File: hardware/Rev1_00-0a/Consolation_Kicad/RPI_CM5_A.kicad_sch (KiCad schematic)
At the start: 56 parts, among them J19 RPI_CMx_A, J7 2998TR, Q12 2N7002, Q13 2N7002, Q15 2N7002, Q16 2N7002, U19 SN74LVC1G125DBVR, U21 MCP7940NT-I/MS, Y2 32.768kHz

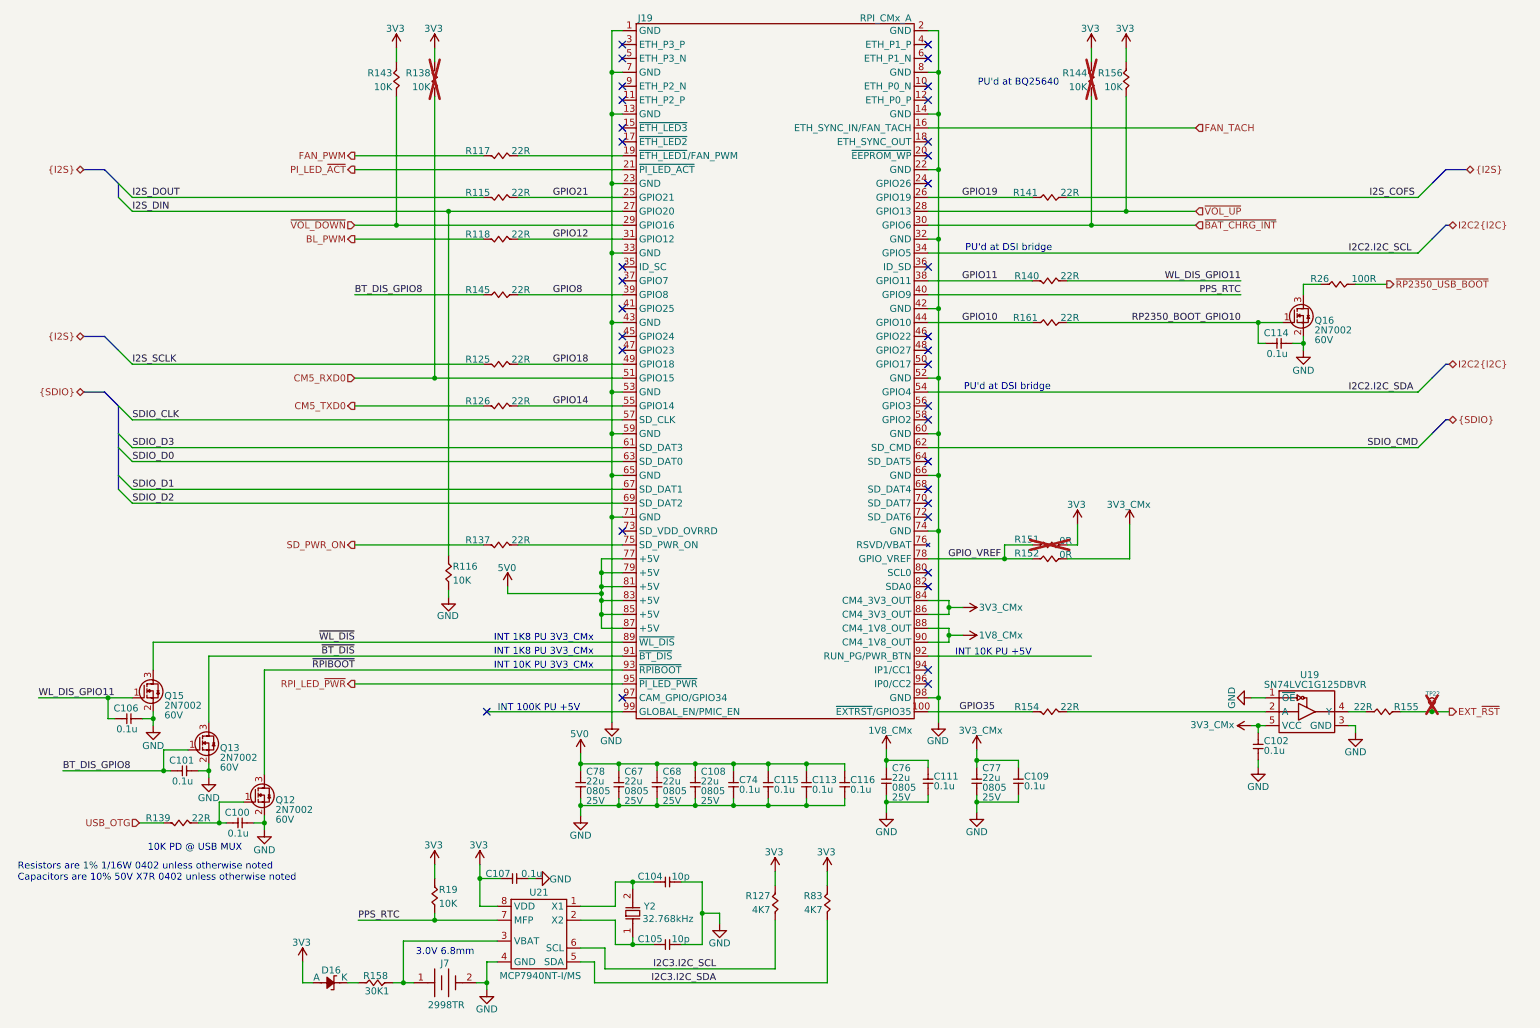
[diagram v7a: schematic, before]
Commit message: Major update to consolation schematics to include - Power supply - RESET SUPERVISOR - Review of GPIO and pinmux
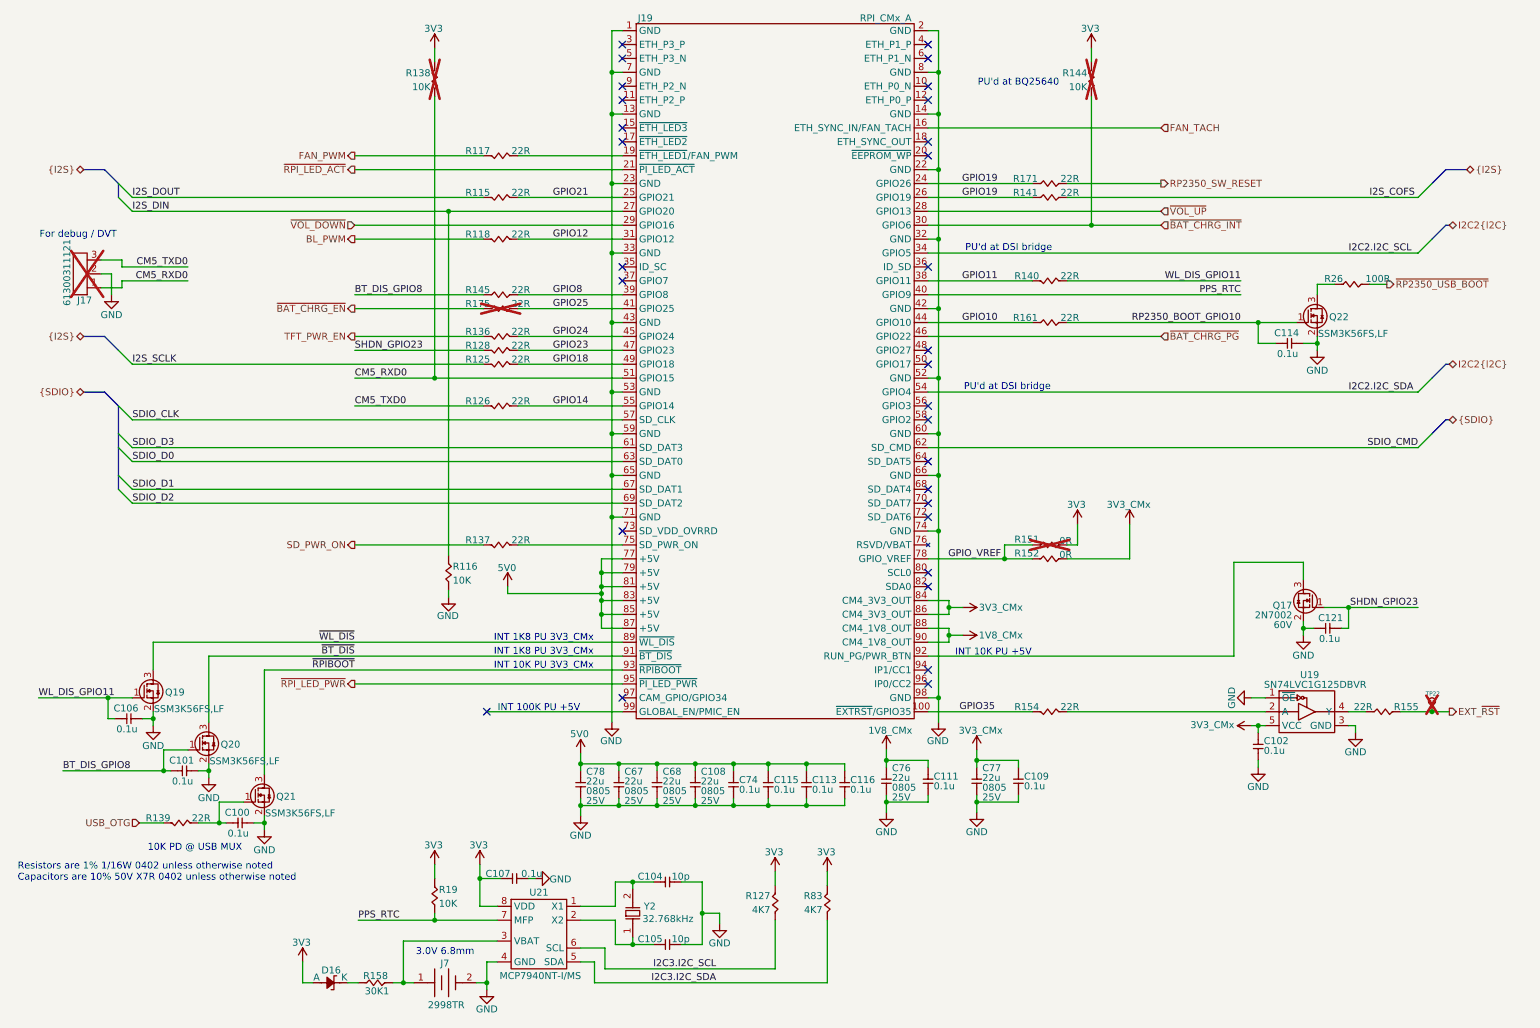
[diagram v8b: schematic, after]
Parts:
- removed Q12, Q13, Q15, Q16: 2N7002, footprint:SOT-23-3, symbol KicadCompDb:Mosfet/MOSFET_00001
- removed R143, R156: 10K, footprint:RES_0402, symbol KicadCompDb:Resistors/RES_SMT_00013
- added C121: 0.1u, footprint:CAP_NONPOL_0402, symbol KicadCompDb:Capacitors/CAP_CER_SMT_00001
- added J17: 61300311121, footprint:HEADER_3P_2_54MM, symbol KicadCompDb:Connector/CONN_00001
- added Q17: 2N7002, footprint:SOT-23-3, symbol KicadCompDb:Mosfet/MOSFET_00001
- added Q19, Q20, Q21, Q22: SSM3K56FS,LF, footprint:SC-75, symbol KicadCompDb:Mosfet/MOSFET_00002
- added R128, R136, R171, R175: 22R, footprint:RES_0402, symbol KicadCompDb:Resistors/RES_SMT_00015
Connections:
- net BT_DIS_GPIO8: now also Q20.1 (G)
- net CM5_RXD0: now also J17.1
- net CM5_TXD0: now also J17.3
- net GND: now also C121.1, J17.2, Q17.2 (S), Q19.2 (S), Q20.2 (S), Q21.2 (S), Q22.2 (S)
- net GPIO19: now also J19.24 (GPIO26), R171.1
- net RP2350_BOOT_GPIO10: now also Q22.1 (G)
- net WL_DIS_GPIO11: now also Q19.1 (G)
- net ~{BT_DIS}: now also Q20.3 (D)
- net ~{RPIBOOT}: now also Q21.3 (D)
- net ~{WL_DIS}: now also Q19.3 (D)
- net at C100.2, R139.1: now also Q21.1 (G)
- net GPIO25: now reaches J19.41 (GPIO25)
- net GPIO25: now also R175.2
- net GPIO24: now reaches J19.45 (GPIO24)
- net GPIO24: now also R136.1
- net ~{BAT_CHRG_PG}: now reaches J19.46 (GPIO22)
- net GPIO23: now reaches J19.47 (GPIO23)
- net GPIO23: now also R128.1
- net at J19.92 (RUN_PG/PWR_BTN): now also Q17.3 (D)
- net at R26.2: now also Q22.3 (D)
- net PI_LED_~{ACT} renamed ~{RPI_LED_ACT}
- net RPI_LED_~{PWR} renamed ~{RPI_LED_PWR}
- new net RP2350_SW_RESET: R171.2
- new net SHDN_GPIO23: C121.2, Q17.1 (G), R128.2
- new net TFT_PWR_EN: R136.2
- new net ~{BAT_CHRG_EN}: R175.1
- no-connect marks 35 -> 30
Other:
- note added: "For debug / DVT"
- moved on the sheet: C114, R26
